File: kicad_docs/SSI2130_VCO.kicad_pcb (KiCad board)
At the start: 4 copper layers, 55.9 x 78.7 mm, 102 parts, among them J1 tuning controls, J2 1 v/oct inputs, J3 linear FM input, J4 sync input, J5 PWM inputs, J6 power input, J7 waveform outputs, Q1 2N7002, U1 SSI2130, U10 LM4040DBZ-5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

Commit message: reduce amt of weird resistor vals
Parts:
- R10: value 50k -> 49k9
- R12, R14, R16: value 25k -> 49k9
- R13, R15, R17, R19, R20, R21, R28: value 100k -> 200k
- R26, R27: value 110k -> 220k
- R29: value 25k -> 51k
- R41: value 499k -> 470k
- R45: value 267R -> 270R
- R46: value 4k02 -> 3k9
- R47, R49: value 4k75 -> 4k7
- R48: value 12k7 -> 12k

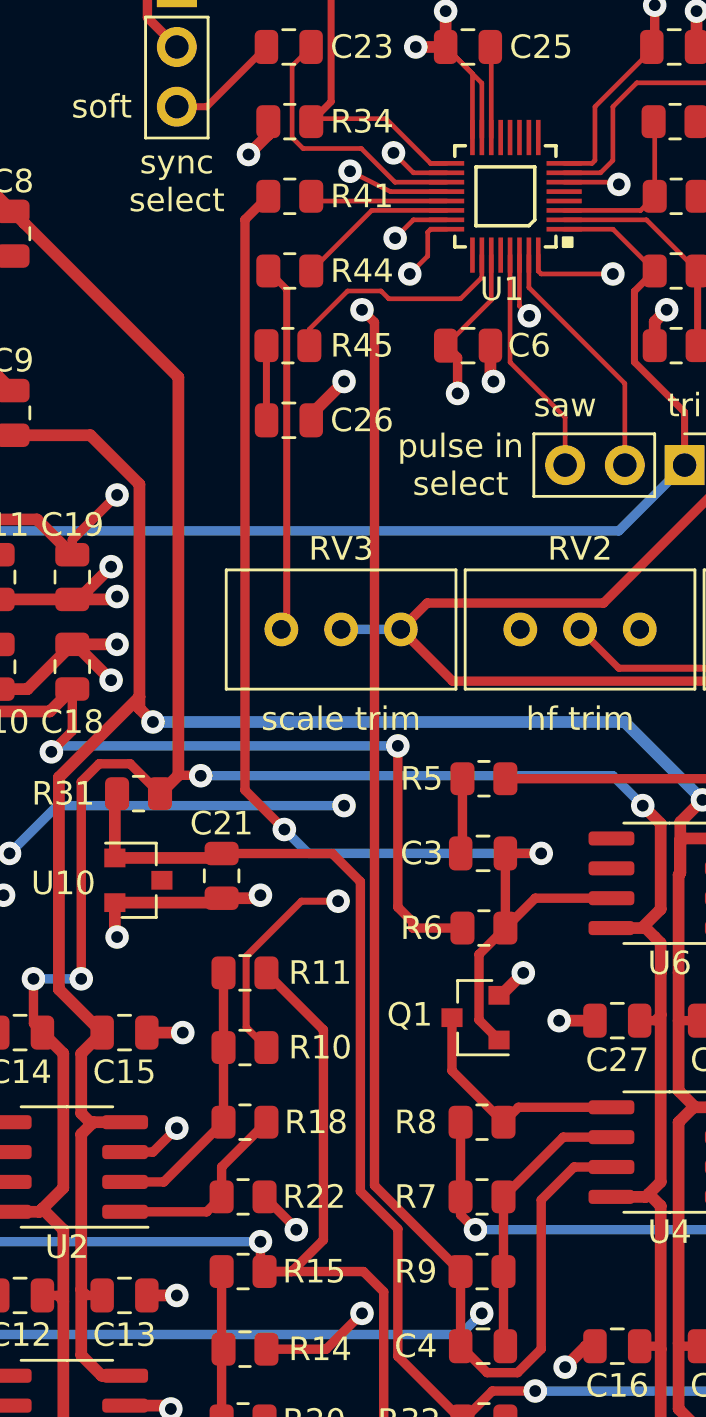
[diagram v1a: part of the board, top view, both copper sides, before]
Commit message: fix error where wires were crossed
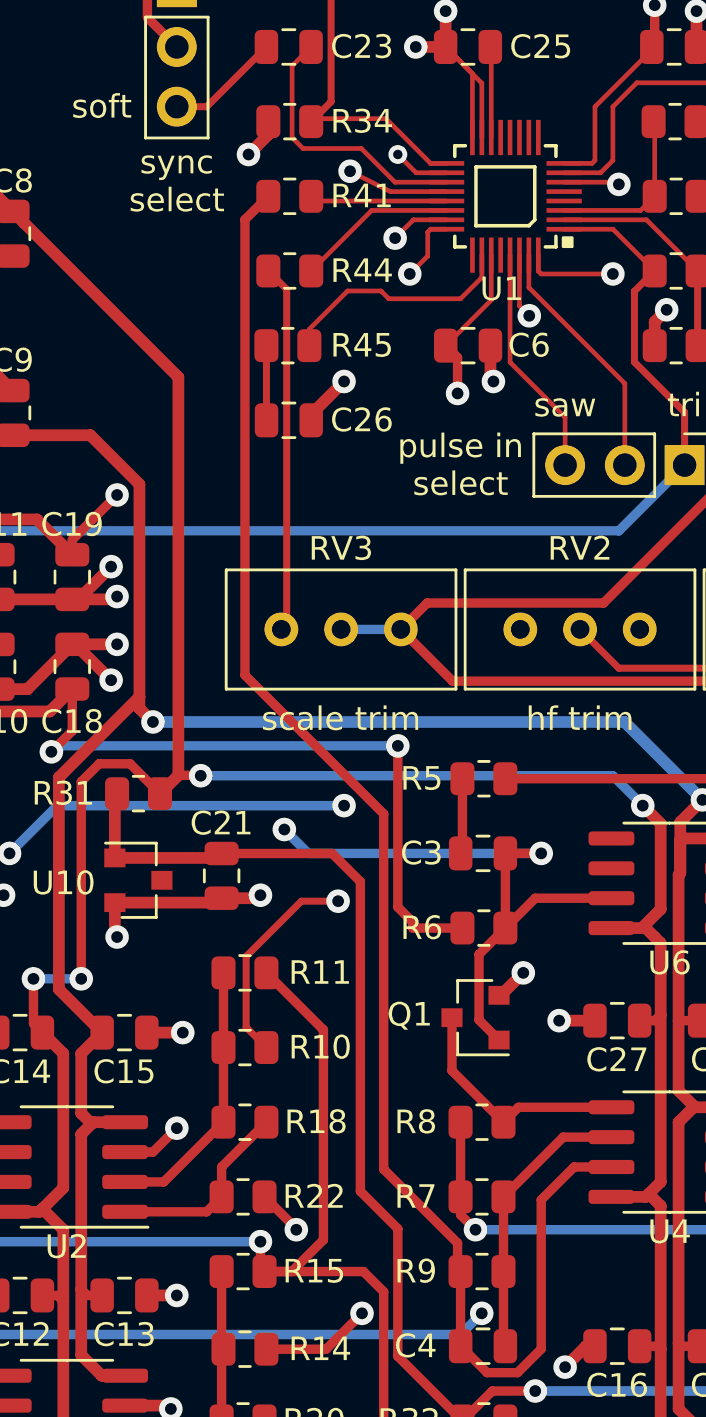
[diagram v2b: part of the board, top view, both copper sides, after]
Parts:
- C5: value 1n -> 10n
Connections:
- C3 pad 1: /VCO_core/lin_FM_in -> /VCO_core/time_rev_in
- C4 pad 1: /tzfm_conditioner/lin_fm_out -> /VCO_core/lin_FM_in
- Q1 pad 1: /VCO_core/lin_FM_in -> /VCO_core/time_rev_in
- R6 pad 1: /VCO_core/lin_FM_in -> /VCO_core/time_rev_in
- R9 pad 1: /tzfm_conditioner/lin_fm_out -> /VCO_core/lin_FM_in
- U1 pad 18: /tzfm_conditioner/lin_fm_out -> /VCO_core/time_rev_in
- U4 pad 7: /tzfm_conditioner/lin_fm_out -> /VCO_core/lin_FM_in
- U6 pad 7: /VCO_core/lin_FM_in -> /VCO_core/time_rev_in
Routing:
- net /tzfm_conditioner/lin_fm_out: track 69.9 -> 0.00 mm, vias 2 -> 0
- net /VCO_core/time_rev_in: track 0.00 -> 60.8 mm, vias 0 -> 3
- net /VCO_core/lin_FM_in: track 54.7 -> 67.3 mm, vias 2 -> 0

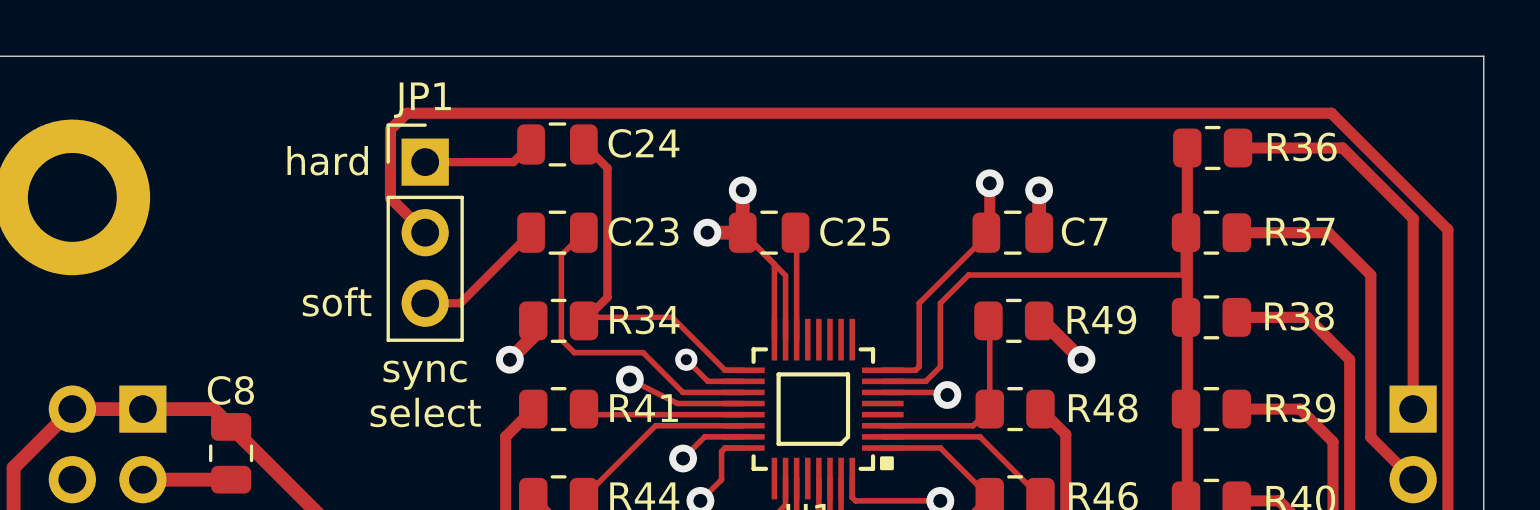
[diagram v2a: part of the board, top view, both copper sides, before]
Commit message: add kick-start network to ensure start up
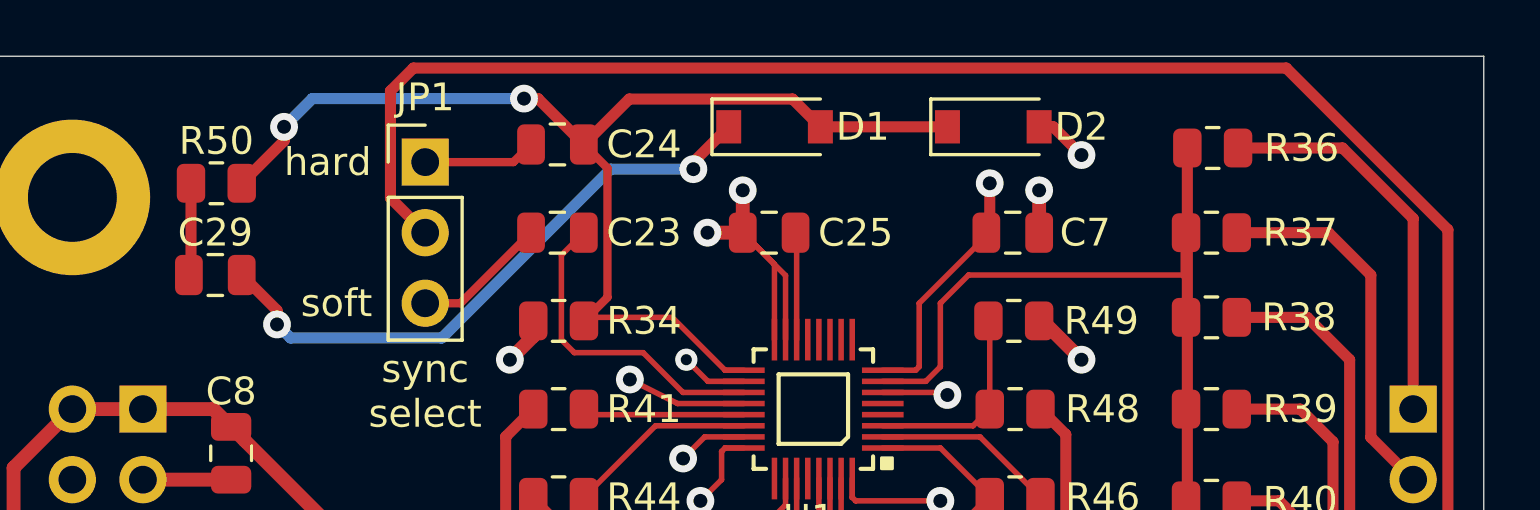
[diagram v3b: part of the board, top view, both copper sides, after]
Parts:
- added C29: 10u, Capacitor_SMD:C_0805_2012Metric, F.Cu at (35.6, 33.3)
- added D1: 1N4148W, Diode_SMD:D_SOD-123, F.Cu at (55.8, 27.9)
- added D2: 1N4148W, Diode_SMD:D_SOD-123, F.Cu at (63.6, 27.9)
- added R50: 10k, Resistor_SMD:R_0805_2012Metric, F.Cu at (35.7, 30.0)
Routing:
- net +5V: track 62.0 -> 110.7 mm, vias 3 -> 5
- net Net-(C24-Pad1): track 13.6 -> 42.4 mm, vias 0 -> 2
- net Net-(C29-Pad1): track 0.00 -> 3.33 mm
- net /VCO_core/sync_in: track 86.8 -> 89.0 mm
- net GND: track 104.3 -> 106.3 mm, vias 35 -> 36
